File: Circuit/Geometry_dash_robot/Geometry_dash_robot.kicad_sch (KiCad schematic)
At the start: 6 parts, among them Q1 IRF740

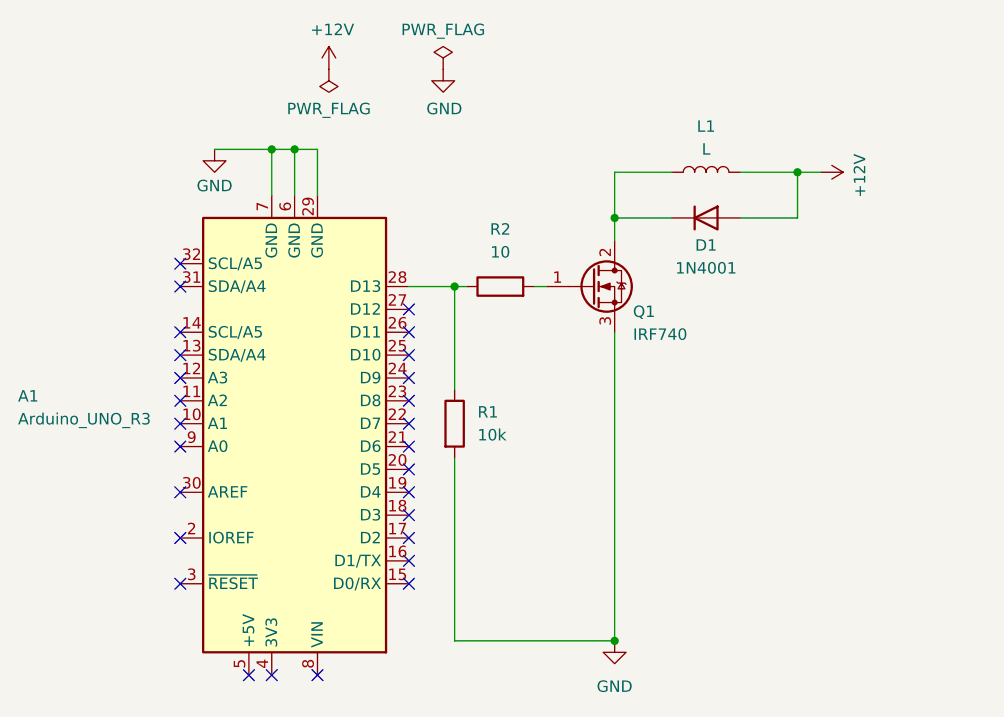
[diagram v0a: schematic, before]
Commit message: deleted Arduino firmware and updated schematic with pb and python with updated pin
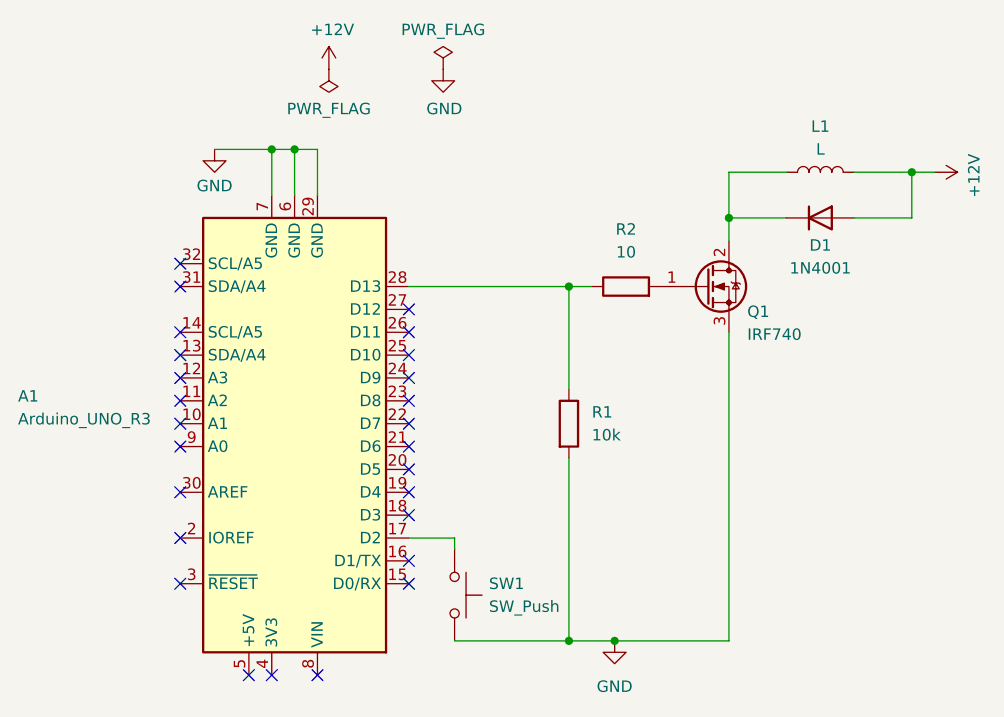
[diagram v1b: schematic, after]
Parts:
- added SW1: SW_Push, symbol Switch:SW_Push
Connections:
- net GND: now also SW1.2
- net at A1.17 (D2): now also SW1.1
- no-connect marks 27 -> 26
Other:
- moved on the sheet: D1, L1, Q1, R1, R2
